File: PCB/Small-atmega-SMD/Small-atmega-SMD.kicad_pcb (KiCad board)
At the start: 2 copper layers, 65.1 x 96.9 mm, 32 parts, among them J1 Daisy port in, J2 ICSP_ISP6, J3 UART, J4 Daisy port out, K1 HYC77-TF09-200, U1 PC817C-S, U2 SE5218, U21 TXB0104QPWRQ1, U3 ATmega328P-AU, Y1 Crystal_GND2

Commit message: Rework for cleanliness
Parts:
- moved R5 29.8 mm to (135.6, 61.2), turned to 0 degrees
- moved R4 24.4 mm to (140.3, 61.0)
- moved D3 19.9 mm to (144.9, 57.3)
- moved U1 19.2 mm to (143.6, 65.0)
- moved D2 19.0 mm to (139.6, 66.2), turned to 0 degrees
- moved R3 12.7 mm to (142.4, 73.3), turned to 90 degrees
- moved J2 9.29 mm to (112.8, 63.3), turned to -90 degrees
- moved R2 8.48 mm to (102.4, 133.6), turned to 0 degrees
- moved J3 6.32 mm to (113.0, 72.3)
- moved C4 6.12 mm to (115.5, 103.2)
- moved REF** 3.59 mm to (108.4, 51.0)
- moved R1 2.77 mm to (135.3, 112.7)
- moved U2 2.53 mm to (111.9, 103.2)
- moved R6 2.23 mm to (111.8, 106.0), turned to 0 degrees
- moved D4 1.73 mm to (104.6, 136.9), turned to 180 degrees
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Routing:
- net 5V_burgerDisk: track 158.0 -> 111.3 mm, vias 8 -> 6
- net LED: track 108.0 -> 79.3 mm, vias 0 -> 2
- net DRV2_burgerDisk: track 33.8 -> 6.95 mm, vias 2 -> 0
- net WRPROT_out: track 90.2 -> 68.0 mm, vias 5 -> 1
- net SCK: track 84.0 -> 71.4 mm, vias 3 -> 1
- net WRPROT_in: track 4.50 -> 15.5 mm, vias 0 -> 2
- net PH0: track 72.3 -> 62.4 mm
- net PH2: track 70.1 -> 60.8 mm
- net PH1: track 69.8 -> 60.7 mm
- net MISO: track 77.4 -> 69.1 mm, vias 3 -> 1
- net GND: track 57.7 -> 49.9 mm, vias 9 -> 7
- net WREQ: track 60.3 -> 66.6 mm
- net -12V: track 59.0 -> 65.1 mm, vias 1 -> 0
- net TX: track 16.8 -> 11.0 mm, vias 1 -> 2
- net MOSI: track 72.8 -> 67.4 mm, vias 3 -> 1
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
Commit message: Let the OCD win
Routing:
- net GND: vias 7 -> 13
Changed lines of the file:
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@@
+	)
+	(via
+		(at 120.6754 62.7126)
+		(size 0.6)
+		(drill 0.3)
+		(layers "F.Cu" "B.Cu")
+		(free yes)
+		(net 2)
+	)
+	(via
+		(at 123.1392 69.2658)
+		(size 0.6)
+		(drill 0.3)
+		(layers "F.Cu" "B.Cu")
+		(free yes)
+		(net 2)
 	)
 	(via
@@
 		(drill 0.3)
 		(layers "F.Cu" "B.Cu")
+		(net 2)
+	)
+	(via
+		(at 132.1054 69.6722)
+		(size 0.6)
+		(drill 0.3)
+		(layers "F.Cu" "B.Cu")
+		(free yes)
+		(net 2)
+	)
+	(via
+		(at 117.348 75.692)
+		(size 0.6)
+		(drill 0.3)
+		(layers "F.Cu" "B.Cu")
+		(free yes)
 		(net 2)
 	)
@@
 	(via
 		(at 137.6426 58.42)
+		(size 0.6)
+		(drill 0.3)
+		(layers "F.Cu" "B.Cu")
+		(free yes)
+		(net 2)
+	)
+	(via
+		(at 136.7536 64.9732)
 		(size 0.6)
 		(drill 0.3)
@@
 		(net 2)
 	)
+	(via
+		(at 116.078 69.977)
+		(size 0.6)
+		(drill 0.3)
+		(layers "F.Cu" "B.Cu")
+		(free yes)
+		(net 2)
+	)

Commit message: Fix LCSC parts
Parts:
- C8: value 100nF -> 100n
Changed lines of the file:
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@@
 			)
 		)
-		(property "Value" "100nF"
+		(property "Value" "100n"
 			(at 0 1.43 0)
 			(layer "F.Fab")
@@
 			)
 		)
-		(property "LCSC" "C28233"
+		(property "LCSC" "C1590"
 			(at 0 0 0)
 			(unlocked yes)
@@
 			)
 		)
-		(property "LCSC" "C17414"
+		(property "LCSC" "C15401"
 			(at 0 0 0)
 			(unlocked yes)

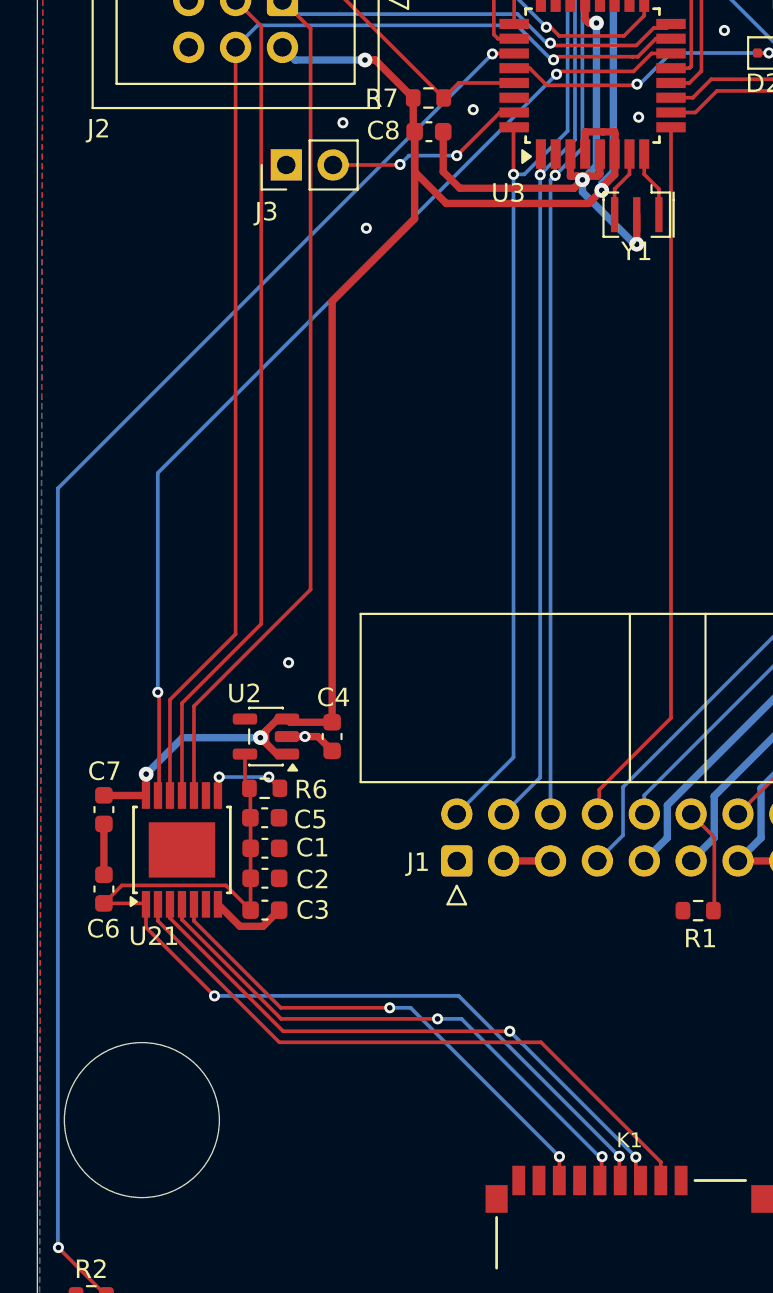
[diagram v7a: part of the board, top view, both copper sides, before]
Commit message: Cleanup caps locations
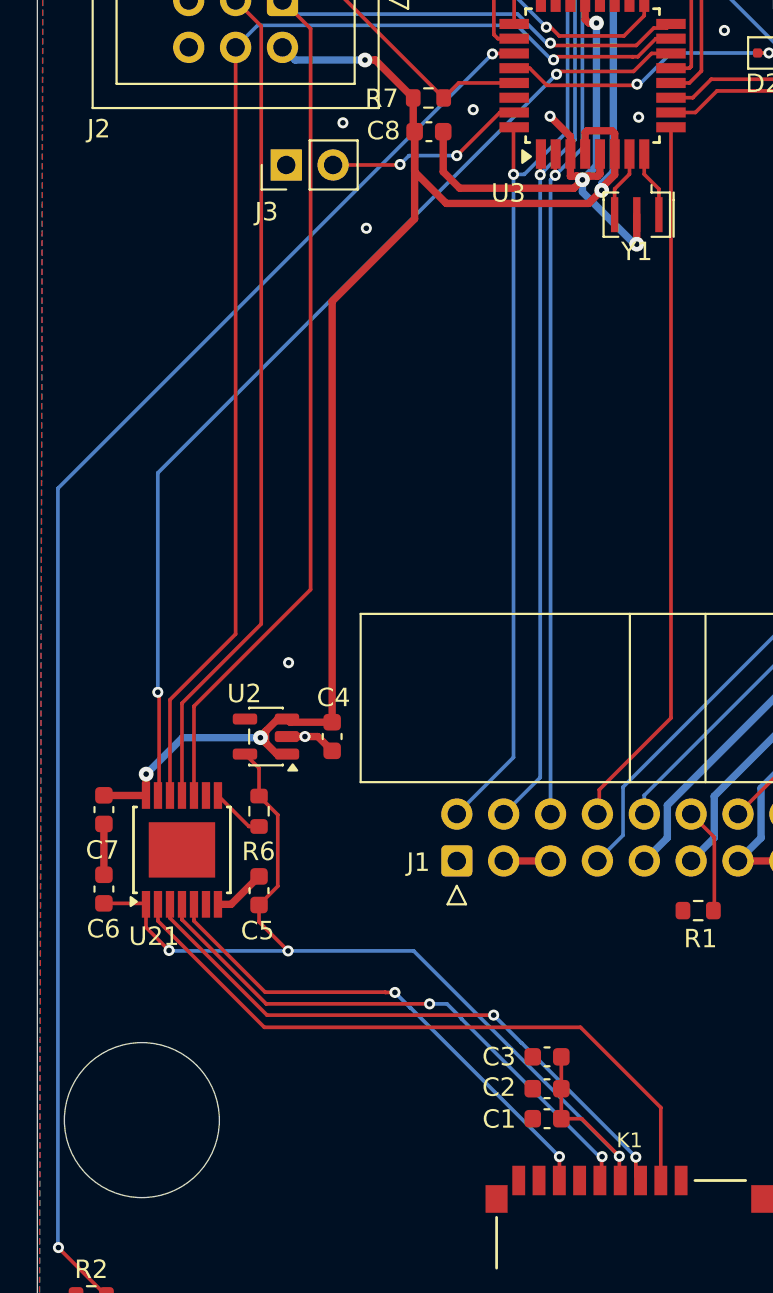
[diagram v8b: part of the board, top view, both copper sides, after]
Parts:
- moved C1 21.2 mm to (127.1, 124.0), turned to 0 degrees
- moved C2 19.1 mm to (127.1, 122.3), turned to 0 degrees
- moved C3 17.2 mm to (127.1, 120.6), turned to 0 degrees
- moved C5 3.96 mm to (111.5, 111.6), turned to -90 degrees
- moved R6 1.28 mm to (111.5, 107.3), turned to -90 degrees
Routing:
- net 3V3: track 53.0 -> 55.4 mm, vias 2 -> 3
- net CS_L: track 34.6 -> 36.3 mm
- net OE: track 4.58 -> 2.92 mm, vias 2 -> 0
- net 5V_burgerDisk: track 111.3 -> 110.0 mm
- net GND: track 49.9 -> 51.1 mm, vias 13 -> 14
